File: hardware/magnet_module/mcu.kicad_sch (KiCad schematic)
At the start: 27 parts, among them J9 STLINK-V3-MINIE, SW1 SW_DIP_x02, SW2 CK_PTS526_SK15_Switch, SW3 CK_PTS526_SK15_Switch, U3 W25Q16JVSSIQ, U8 STM32G474RETx, U9 TXB0102RUT

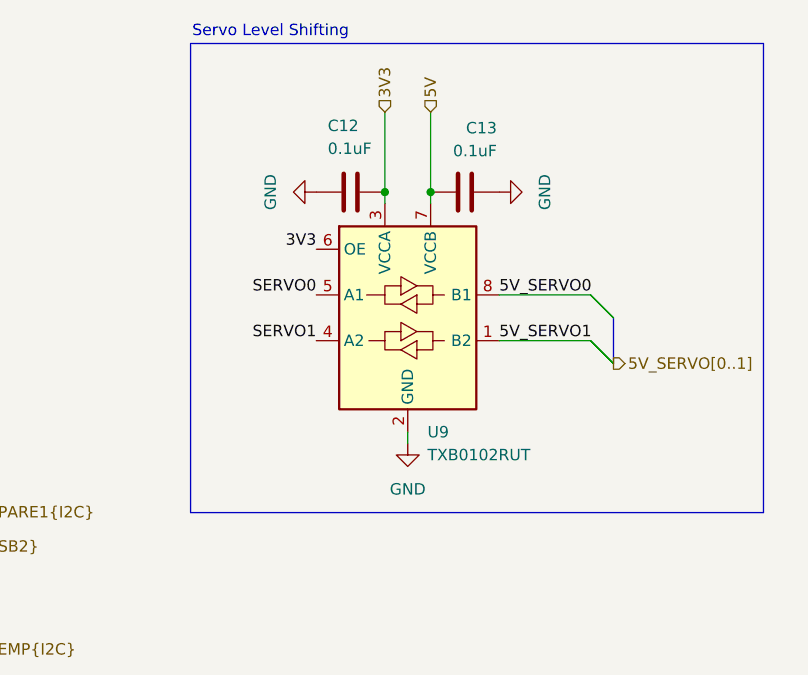
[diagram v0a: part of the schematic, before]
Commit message: change power LED brightness, move level shifter to servo page
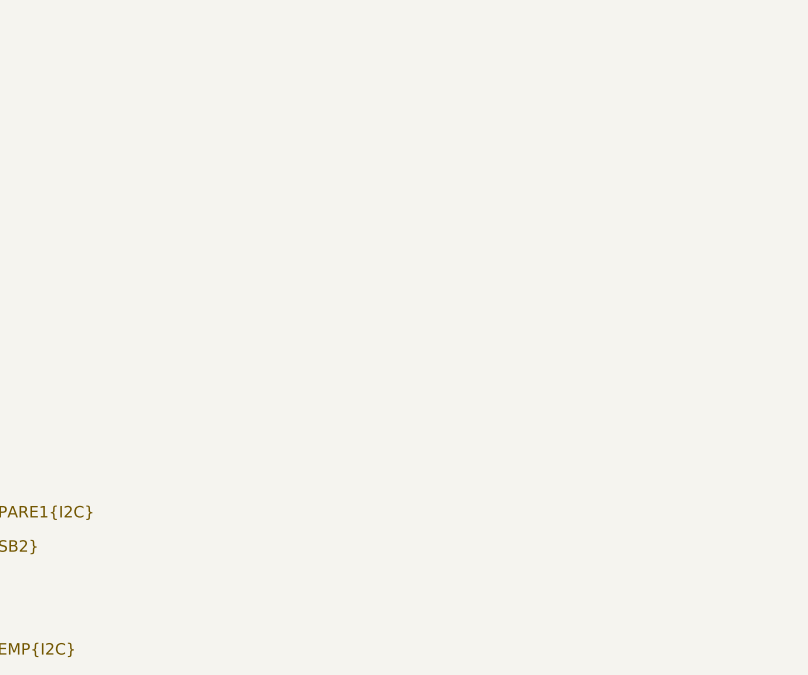
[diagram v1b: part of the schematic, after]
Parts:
- removed C12, C13: 0.1uF, symbol Device:C
- removed U9: TXB0102RUT, Package_SO:TSSOP-8_3x3mm_P0.65mm, symbol Logic_LevelTranslator:TXB0102DCT
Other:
- note removed: "Servo Level Shifting"

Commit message: add titles & esd protection for IO
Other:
- company: (none) -> Christie Lab, CU-Anschultz
- title: (none) -> Autotrainer Magnet Module - MCU
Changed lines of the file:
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@@
 	(generator_version "8.0")
 	(paper "A4")
+	(title_block
+		(title "Autotrainer Magnet Module - MCU")
+		(date "2024-07-09")
+		(rev "v1.0")
+		(company "Christie Lab, CU-Anschultz")
+		(comment 1 "Prepared by LeafLabs, LLC")
+	)
 	(bus_alias "FDCAN"
 		(members "RX" "TX")

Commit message: add all PNs, relevant datasheets, and test points
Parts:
- added TP10, TP11: TestPoint, symbol Connector:TestPoint
- C10, C11, C14, C15, C16, C17, C18, C19: footprint (none) -> Capacitor_SMD:C_0603_1608Metric; MPN (none) -> CC0603KRX7R7BB104
- D2: footprint (none) -> Diode_SMD:D_0603_1608Metric; MPN (none) -> 150060YS75000
- FB1, FB2: footprint (none) -> Inductor_SMD:L_0603_1608Metric; MPN (none) -> BLM18KG121TN1D
- J9: MPN (none) -> FTSH-107-01-F-D-K
- R10, R11, R7, R8, R9: MPN (none) -> RC0603FR-0710KL
- R14: MPN (none) -> RC0603FR-07220RL
- SW1: MPN (none) -> DS04-254-2-02BK-SMT
- U3: MPN (none) -> W25Q16JVSSIQ
- U8: MPN (none) -> STM32G474RET6
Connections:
- net BOOT: now also TP10.1
- net ~{MCU_RST}: now also TP11.1

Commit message: make changes as requested by Ryan
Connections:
- net STIM0: no longer names the net of U8.52 (PC10)
- net STIM1: no longer names the net of U8.53 (PC11)
- net STIM2: no longer names the net of U8.54 (PC12)
- no-connect marks 18 -> 21
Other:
- company: Christie Lab, CU-Anschultz -> Christie Lab, CU-Anschutz
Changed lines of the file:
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@@
 		(date "2024-07-09")
 		(rev "v1.0")
-		(company "Christie Lab, CU-Anschultz")
+		(company "Christie Lab, CU-Anschutz")
 		(comment 1 "Prepared by LeafLabs, LLC")
 	)
@@
 	)
 	(no_connect
+		(at 135.89 96.52)
+	)
+	(no_connect
 		(at 135.89 76.2)
 	)
@@
 	)
 	(no_connect
+		(at 135.89 93.98)
+	)
+	(no_connect
 		(at 171.45 55.88)
+	)
+	(no_connect
+		(at 135.89 91.44)
 	)
 	(bus_entry
@@
 	)
 	(bus_entry
-		(at 121.92 99.06)
-		(size 2.54 -2.54)
-		(stroke
-			(width 0)
-			(type default)
-		)
-	)
-	(bus_entry
 		(at 109.22 83.82)
 		(size 2.54 2.54)
@@
 	)
 	(bus_entry
-		(at 121.92 93.98)
-		(size 2.54 -2.54)
-		(stroke
-			(width 0)
-			(type default)
-		)
-	)
-	(bus_entry
 		(at 200.66 93.98)
 		(size -2.54 -2.54)
-		(stroke
-			(width 0)
-			(type default)
-		)
-	)
-	(bus_entry
-		(at 121.92 96.52)
-		(size 2.54 -2.54)
 		(stroke
 			(width 0)
@@
 	(wire
 		(pts
-			(xy 124.46 96.52) (xy 135.89 96.52)
+			(xy 171.45 88.9) (xy 198.12 88.9)
+		)
+		(stroke
+			(width 0)
+			(type default)
+		)
+	)
+	(wire
+		(pts
+			(xy 140.97 177.8) (xy 132.08 177.8)
 		)
 		(stroke
@@
 	(bus
 		(pts
-			(xy 121.92 96.52) (xy 121.92 99.06)
-		)
-		(stroke
-			(width 0)
-			(type default)
-		)
-	)
-	(wire
-		(pts
-			(xy 171.45 88.9) (xy 198.12 88.9)
-		)
-		(stroke
-			(width 0)
-			(type default)
-		)
-	)
-	(wire
-		(pts
-			(xy 140.97 177.8) (xy 132.08 177.8)
-		)
-		(stroke
-			(width 0)
-			(type default)
-		)
-	)
-	(wire
-		(pts
-			(xy 124.46 91.44) (xy 135.89 91.44)
+			(xy 109.22 83.82) (xy 109.22 86.36)
 		)
 		(stroke
@@
 	(bus
 		(pts
-			(xy 109.22 83.82) (xy 109.22 86.36)
+			(xy 194.31 83.82) (xy 195.58 83.82)
+		)
+		(stroke
+			(width 0)
+			(type default)
+		)
+	)
+	(wire
+		(pts
+			(xy 140.97 177.8) (xy 144.78 177.8)
+		)
+		(stroke
+			(width 0)
+			(type default)
+		)
+	)
+	(wire
+		(pts
+			(xy 156.21 38.1) (xy 156.21 36.83)
+		)
+		(stroke
+			(width 0)
+			(type default)
+		)
+	)
+	(wire
+		(pts
+			(xy 245.11 149.86) (xy 217.17 149.86)
+		)
+		(stroke
+			(width 0)
+			(type default)
+		)
+	)
+	(wire
+		(pts
+			(xy 20.32 110.49) (xy 20.32 111.76)
+		)
+		(stroke
+			(width 0)
+			(type default)
+		)
+	)
+	(wire
+		(pts
+			(xy 57.15 111.76) (xy 57.15 113.03)
+		)
+		(stroke
+			(width 0)
+			(type default)
+		)
+	)
+	(wire
+		(pts
+			(xy 20.32 110.49) (xy 21.59 110.49)
+		)
+		(stroke
+			(width 0)
+			(type default)
+		)
+	)
+	(wire
+		(pts
+			(xy 160.02 175.26) (xy 160.02 177.8)
 		)
 		(stroke
@@
 	(bus
 		(pts
-			(xy 194.31 83.82) (xy 195.58 83.82)
-		)
-		(stroke
-			(width 0)
-			(type default)
-		)
-	)
-	(wire
-		(pts
-			(xy 140.97 177.8) (xy 144.78 177.8)
-		)
-		(stroke
-			(width 0)
-			(type default)
-		)
-	)
-	(wire
-		(pts
-			(xy 156.21 38.1) (xy 156.21 36.83)
-		)
-		(stroke
-			(width 0)
-			(type default)
-		)
-	)
-	(wire
-		(pts
-			(xy 245.11 149.86) (xy 217.17 149.86)
-		)
-		(stroke
-			(width 0)
-			(type default)
-		)
-	)
-	(wire
-		(pts
-			(xy 20.32 110.49) (xy 20.32 111.76)
-		)
-		(stroke
-			(width 0)
-			(type default)
-		)
-	)
-	(wire
-		(pts
-			(xy 57.15 111.76) (xy 57.15 113.03)
-		)
-		(stroke
-			(width 0)
-			(type default)
-		)
-	)
-	(wire
-		(pts
-			(xy 20.32 110.49) (xy 21.59 110.49)
-		)
-		(stroke
-			(width 0)
-			(type default)
-		)
-	)
-	(wire
-		(pts
-			(xy 160.02 175.26) (xy 160.02 177.8)
+			(xy 189.23 100.33) (xy 189.23 101.6)
+		)
+		(stroke
+			(width 0)
+			(type default)
+		)
+	)
+	(wire
+		(pts
+			(xy 255.27 128.27) (xy 270.51 128.27)
+		)
+		(stroke
+			(width 0)
+			(type default)
+		)
+	)
+	(wire
+		(pts
+			(xy 26.67 85.09) (xy 26.67 87.63)
 		)
 		(stroke
@@
 	(bus
 		(pts
-			(xy 189.23 100.33) (xy 189.23 101.6)
-		)
-		(stroke
-			(width 0)
-			(type default)
-		)
-	)
-	(wire
-		(pts
-			(xy 255.27 128.27) (xy 270.51 128.27)
-		)
-		(stroke
-			(width 0)
-			(type default)
-		)
-	)
-	(wire
-		(pts
-			(xy 26.67 85.09) (xy 26.67 87.63)
+			(xy 194.31 73.66) (xy 194.31 76.2)
+		)
+		(stroke
+			(width 0)
+			(type default)
+		)
+	)
+	(wire
+		(pts
+			(xy 156.21 36.83) (xy 153.67 36.83)
+		)
+		(stroke
+			(width 0)
+			(type default)
+		)
+	)
+	(wire
+		(pts
+			(xy 130.81 78.74) (xy 135.89 78.74)
 		)
 		(stroke
@@
 	(bus
 		(pts
-			(xy 194.31 73.66) (xy 194.31 76.2)
-		)
-		(stroke
-			(width 0)
-			(type default)
-		)
-	)
-	(wire
-		(pts
-			(xy 156.21 36.83) (xy 153.67 36.83)
-		)
-		(stroke
-			(width 0)
-			(type default)
-		)
-	)
-	(wire
-		(pts
-			(xy 130.81 78.74) (xy 135.89 78.74)
-		)
-		(stroke
-			(width 0)
-			(type default)
-		)
-	)
-	(wire
-		(pts
-			(xy 124.46 93.98) (xy 135.89 93.98)
-		)
-		(stroke
-			(width 0)
-			(type default)
-		)
-	)
-	(bus
-		(pts
 			(xy 195.58 66.04) (xy 195.58 68.58)
-		)
-		(stroke
-			(width 0)
-			(type default)
-		)
-	)
-	(bus
-		(pts
-			(xy 121.92 93.98) (xy 121.92 96.52)
 		)
 		(stroke
@@
 		)
 	)
-	(label "STIM1"
-		(at 124.46 93.98 0)
-		(fields_autoplaced yes)
-		(effects
-			(font
-				(size 1.27 1.27)
-			)
-			(justify left bottom)
-		)
-	)
 	(label "SERVO1"
 		(at 171.45 50.8 0)
@@
 		)
 	)
-	(label "STIM2"
-		(at 124.46 96.52 0)
-		(fields_autoplaced yes)
-		(effects
-			(font
-				(size 1.27 1.27)
-			)
-			(justify left bottom)
-		)
-	)
 	(label "3V3"
 		(at 217.17 138.43 90)
@@
 	(label "SPARE1.SDA"
 		(at 171.45 63.5 0)
-		(fields_autoplaced yes)
-		(effects
-			(font
-				(size 1.27 1.27)
-			)
-			(justify left bottom)
-		)
-	)
-	(label "STIM0"
-		(at 124.46 91.44 0)
 		(fields_autoplaced yes)
 		(effects
@@
 		(fields_autoplaced yes)
 		(effects
-			(font
-				(size 1.27 1.27)
-			)
-			(justify right)
-		)
-	)
-	(hierarchical_label "STIM[0..3]"
-		(shape bidirectional)
-		(at 121.92 99.06 180)
-		(fields_autoplaced yes)
-		(effects

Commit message: make changes requested by dan, run ERC
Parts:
- TP10, TP11: now fitted; now left out of the parts list
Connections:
- net STIM3: no longer names the net of U8.55 (PD2)
- no-connect marks 21 -> 22
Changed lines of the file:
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@@
 	)
 	(no_connect
+		(at 135.89 60.96)
+	)
+	(no_connect
 		(at 58.42 72.39)
 	)
@@
 	)
 	(bus_entry
+		(at 199.39 45.72)
+		(size -2.54 2.54)
+		(stroke
+			(width 0)
+			(type default)
+		)
+	)
+	(bus_entry
 		(at 109.22 83.82)
 		(size 2.54 2.54)
@@
 	)
 	(bus_entry
+		(at 199.39 48.26)
+		(size -2.54 2.54)
+		(stroke
+			(width 0)
+			(type default)
+		)
+	)
+	(bus_entry
 		(at 194.31 76.2)
 		(size -2.54 -2.54)
@@
 		)
 	)
+	(bus
+		(pts
+			(xy 199.39 45.72) (xy 199.39 48.26)
+		)
+		(stroke
+			(width 0)
+			(type default)
+		)
+	)
 	(wire
 		(pts
@@
 		)
 	)
+	(wire
+		(pts
+			(xy 171.45 48.26) (xy 196.85 48.26)
+		)
+		(stroke
+			(width 0)
+			(type default)
+		)
+	)
 	(bus
 		(pts
@@
 	(wire
 		(pts
+			(xy 171.45 50.8) (xy 196.85 50.8)
+		)
+		(stroke
+			(width 0)
+			(type default)
+		)
+	)
+	(wire
+		(pts
 			(xy 245.11 149.86) (xy 217.17 149.86)
 		)
@@
 		)
 	)
-	(label "STIM3"
-		(at 135.89 60.96 180)
-		(fields_autoplaced yes)
-		(effects
-			(font
-				(size 1.27 1.27)
-			)
-			(justify right bottom)
-		)
-	)
 	(label "SWCLK"
 		(at 171.45 78.74 0)
@@
 		)
 	)
+	(hierarchical_label "SERVO[0..1]"
+		(shape output)
+		(at 199.39 45.72 0)
+		(fields_autoplaced yes)
+		(effects
+			(font
+				(size 1.27 1.27)
+			)
+			(justify left)
+		)
+	)
 	(hierarchical_label "{USB2}"
 		(shape bidirectional)
@@
 		(unit 1)
 		(exclude_from_sim no)
-		(in_bom yes)
+		(in_bom no)
 		(on_board yes)
-		(dnp yes)
+		(dnp no)
 		(fields_autoplaced yes)
 		(property "Reference" "TP10"
@@
 		(unit 1)
 		(exclude_from_sim no)
-		(in_bom yes)
+		(in_bom no)
 		(on_board yes)
-		(dnp yes)
+		(dnp no)
 		(fields_autoplaced yes)
 		(property "Reference" "TP11"

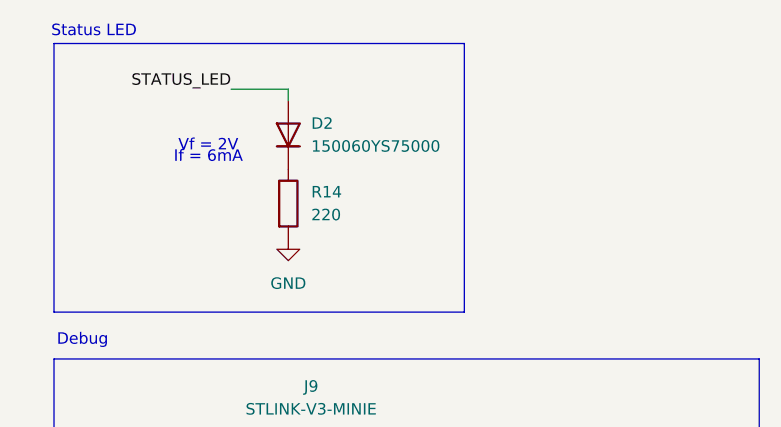
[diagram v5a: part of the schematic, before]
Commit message: add footprints & 3d models for magnet module connector placmeent
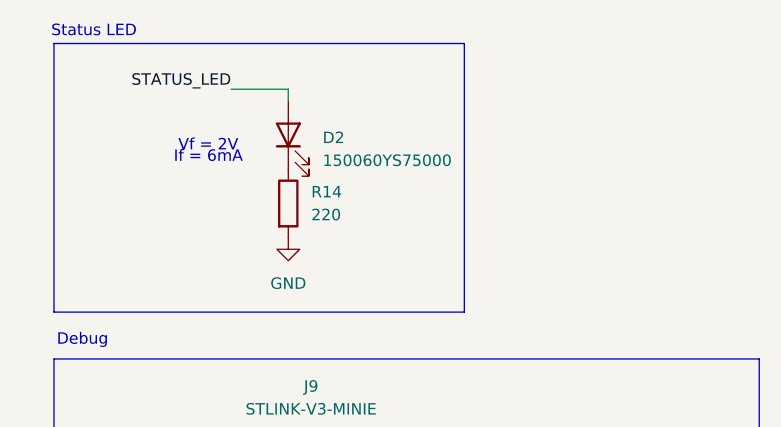
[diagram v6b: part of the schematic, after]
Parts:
- D2: symbol Device:D -> Device:LED
- R10, R11, R14, R7, R8, R9: footprint (none) -> Resistor_SMD:R_0603_1608Metric
- SW1: footprint (none) -> Package_DIP:DIP-4_W8.89mm_SMDSocket_LongPads
- TP10, TP11: footprint (none) -> TestPoint:TestPoint_Pad_1.0x1.0mm
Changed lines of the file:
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@@
 			)
 		)
-		(property "Footprint" ""
+		(property "Footprint" "Package_DIP:DIP-4_W8.89mm_SMDSocket_LongPads"
 			(at 152.4 177.8 0)
 			(effects
@@
 			)
 		)
-		(property "Footprint" ""
+		(property "Footprint" "TestPoint:TestPoint_Pad_1.0x1.0mm"
 			(at 73.66 114.3 0)
 			(effects
@@
 			)
 		)
-		(property "Footprint" ""
+		(property "Footprint" "Resistor_SMD:R_0603_1608Metric"
 			(at 218.948 142.24 90)
 			(effects
@@
 			)
 		)
-		(property "Footprint" ""
+		(property "Footprint" "Resistor_SMD:R_0603_1608Metric"
 			(at 139.7 184.912 90)
 			(effects
@@
 			)
 		)
-		(property "Footprint" ""
+		(property "Footprint" "Resistor_SMD:R_0603_1608Metric"
 			(at 227.838 142.24 90)
 			(effects
@@
 			)
 		)
-		(property "Footprint" ""
+		(property "Footprint" "Resistor_SMD:R_0603_1608Metric"
 			(at 142.748 166.37 90)
 			(effects
@@
 			)
 		)
-		(property "Footprint" ""
+		(property "Footprint" "Resistor_SMD:R_0603_1608Metric"
 			(at 38.862 34.29 90)
 			(effects
@@
 	)
 	(symbol
-		(lib_id "Device:D")
+		(lib_id "Device:LED")
 		(at 40.64 26.67 90)
 		(unit 1)
@@
 		(fields_autoplaced yes)
 		(property "Reference" "D2"
-			(at 43.18 25.3999 90)
+			(at 44.45 26.9874 90)
 			(effects
 				(font
@@
 		)
 		(property "Value" "150060YS75000"
-			(at 43.18 27.9399 90)
+			(at 44.45 29.5274 90)
 			(effects
 				(font
@@
 			)
 		)
-		(property "Description" "Diode"
+		(property "Description" "Light emitting diode"
 			(at 40.64 26.67 0)
 			(effects
@@
 		(pin "45"
 		)
+		(instances
+			(project ""
+				(path "/aa5044b8-67cd-4b5a-a593-0df9431eb095/286cc8bf-34fd-48cd-9d6c-58653d0694aa"
+					(reference "U8")
+					(unit 1)
+				)
+			)
+		)
 	)
 	(symbol
@@
 			)
 		)
-		(property "Footprint" ""
+		(property "Footprint" "Resistor_SMD:R_0603_1608Metric"
 			(at 134.112 166.37 90)
 			(effects
@@
 			)
 		)
-		(property "Footprint" ""
+		(property "Footprint" "TestPoint:TestPoint_Pad_1.0x1.0mm"
 			(at 40.64 113.03 0)
 			(effects

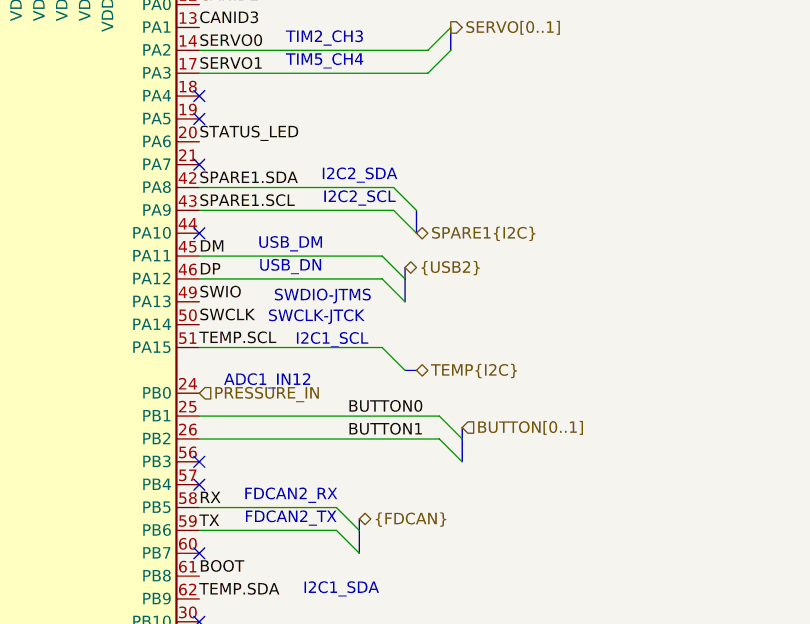
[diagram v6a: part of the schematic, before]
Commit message: Schematic updates to remove button connectors and extra STEMMA QT
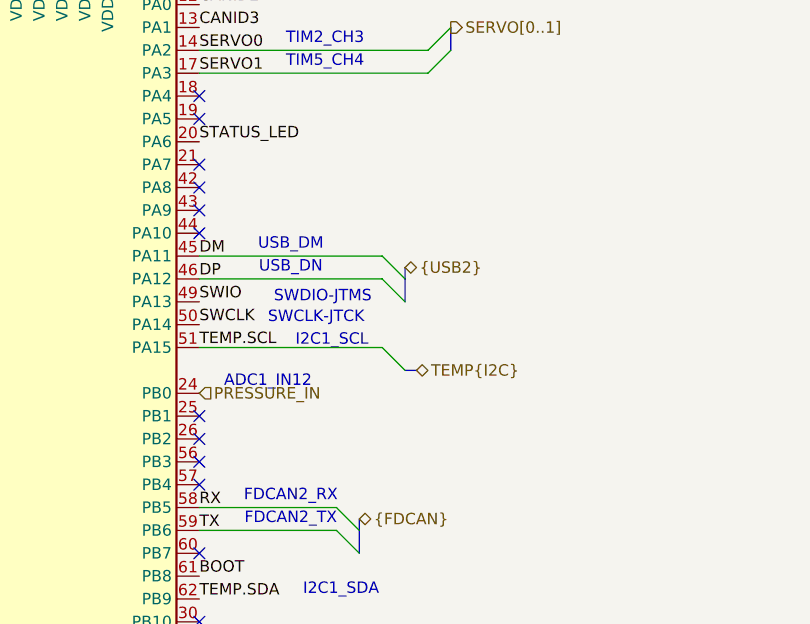
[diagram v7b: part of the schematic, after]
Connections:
- net BUTTON0: no longer names the net of U8.25 (PB1)
- net BUTTON1: no longer names the net of U8.26 (PB2)
- net SPARE1.SCL: no longer names the net of U8.43 (PA9)
- net SPARE1.SDA: no longer names the net of U8.42 (PA8)
- no-connect marks 22 -> 26
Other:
- note removed: "I2C2_SCL"
- note removed: "I2C2_SDA"

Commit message: Releases layout for pellet, magnet, and Jetson breakout boards.
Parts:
- C10, C11, C14, C15, C16, C17, C18, C19: LCSC (none) -> C14663; MPN CC0603KRX7R7BB104 -> CC0603KRX7R9BB104
- D2: LCSC (none) -> C9900012286
- FB1, FB2: LCSC (none) -> C85831
- J9: MPN FTSH-107-01-F-D-K -> (none)
- R10, R11, R7, R8, R9: LCSC (none) -> C25804; MPN RC0603FR-0710KL -> 0603WAF1002T5E
- R14: LCSC (none) -> C22962; MPN RC0603FR-07220RL -> 0603WAF2200T5E
- SW1: LCSC (none) -> C3312172
- SW2, SW3: LCSC (none) -> C2689521
- U3: LCSC (none) -> C82317
- U8: LCSC (none) -> C521608
- XTAL1: LCSC (none) -> C1987194
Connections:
- net DM renamed DN
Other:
- note added: "ADC1_IN15"
- note removed: "ADC1_IN12"
